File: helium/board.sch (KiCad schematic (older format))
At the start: 64 parts, among them J1 Power, J10 OUT B3, J12 IN C, J13 OUT C1, J14 OUT C2, J15 OUT C3, J17 OUT D, J18 IN D1, J19 IN D2, J2 IN A, J20 IN D3, J3 OUT A1, J4 OUT A2, J5 OUT A3, J7 IN B, J8 OUT B1, J9 OUT B2, U1 OPA4991, U2 OPA4991, U4 OPA4991, U6 OPA4991

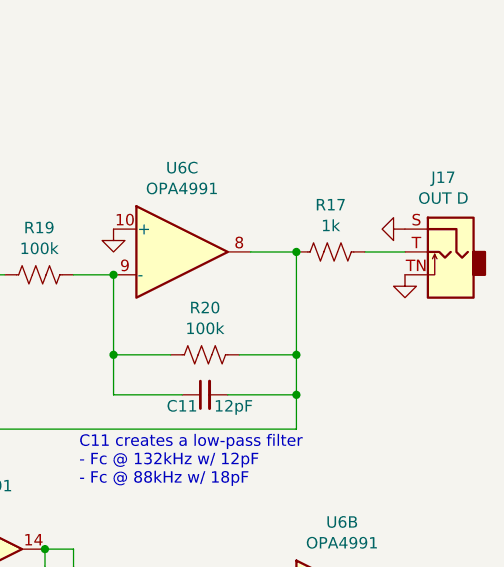
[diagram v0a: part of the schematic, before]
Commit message: Rename folders
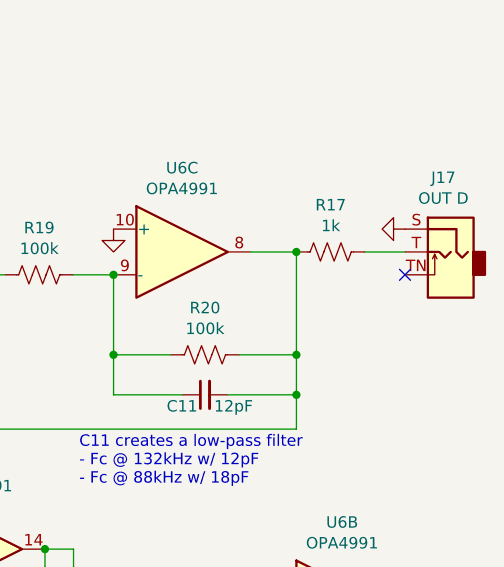
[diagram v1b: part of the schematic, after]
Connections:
- net GND: no longer J17.TN (Tip_normalize)
- no-connect marks 9 -> 10
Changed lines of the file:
@@
 Sheet 1 1
 Title "Helium"
-Date "2021-10-02"
+Date "2021-10-05"
 Rev "v2"
 Comp "Winterbloom"
@@
 Wire Wire Line
 	10550 4375 10725 4375
-$Comp
-L power:GND #PWR0147
-U 1 1 615B5A1D
-P 10725 4475
-F 0 "#PWR0147" H 10725 4225 50  0001 C CNN
-F 1 "GND" H 10730 4302 50  0001 C CNN
-F 2 "" H 10725 4475 50  0001 C CNN
-F 3 "" H 10725 4475 50  0001 C CNN
-	1    10725 4475
-	1    0    0    -1
-$EndComp
 Wire Wire Line
 	8550 2525 8325 2525
@@
 Text Notes 9300 5400 0    50   ~ 0
 C11 creates a low-pass filter\n- Fc @ 132kHz w/ 12pF\n- Fc @ 88kHz w/ 18pF
+NoConn ~ 10725 4475
 $EndSCHEMATC
